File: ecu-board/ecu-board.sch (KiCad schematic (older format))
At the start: 12 parts, among them J1 MicroSquirt_connector, J3 MS_breakout_conn, U1 MAP Sensor

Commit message: Reassign footprints to 0805.
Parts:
- D4, D5: footprint LEDs:LED_D3.0mm -> LEDs:LED_0805_HandSoldering
- R1, R2, R3, R4: footprint Resistors_THT:R_Axial_DIN0309_L9.0mm_D3.2mm_P12.70mm_Horizontal -> Resistors_SMD:R_0805_HandSoldering
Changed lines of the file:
@@
 F 0 "R3" H 8070 1746 50  0000 L CNN
 F 1 "30k" H 8070 1655 50  0000 L CNN
-F 2 "Resistors_THT:R_Axial_DIN0309_L9.0mm_D3.2mm_P12.70mm_Horizontal" V 7930 1700 50  0001 C CNN
+F 2 "Resistors_SMD:R_0805_HandSoldering" V 7930 1700 50  0001 C CNN
 F 3 "~" H 8000 1700 50  0001 C CNN
 	1    8000 1700
@@
 F 0 "R4" H 8070 2146 50  0000 L CNN
 F 1 "30k" H 8070 2055 50  0000 L CNN
-F 2 "Resistors_THT:R_Axial_DIN0309_L9.0mm_D3.2mm_P12.70mm_Horizontal" V 7930 2100 50  0001 C CNN
+F 2 "Resistors_SMD:R_0805_HandSoldering" V 7930 2100 50  0001 C CNN
 F 3 "~" H 8000 2100 50  0001 C CNN
 	1    8000 2100
@@
 F 0 "D4" H 3250 2550 50  0000 C CNN
 F 1 "LED" H 3250 2450 50  0000 C CNN
-F 2 "LEDs:LED_D3.0mm" H 3250 2650 50  0001 C CNN
+F 2 "LEDs:LED_0805_HandSoldering" H 3250 2650 50  0001 C CNN
 F 3 "~" H 3250 2650 50  0001 C CNN
 F 4 "3mm T-1" H 3250 2650 50  0001 C CNN "Part no."
@@
 F 0 "R1" V 3015 2650 50  0000 C CNN
 F 1 "1k" V 3106 2650 50  0000 C CNN
-F 2 "Resistors_THT:R_Axial_DIN0309_L9.0mm_D3.2mm_P12.70mm_Horizontal" V 2830 2650 50  0001 C CNN
+F 2 "Resistors_SMD:R_0805_HandSoldering" V 2830 2650 50  0001 C CNN
 F 3 "~" H 2900 2650 50  0001 C CNN
 	1    2900 2650
@@
 F 0 "D5" H 5350 2500 50  0000 C CNN
 F 1 "LED" H 5350 2400 50  0000 C CNN
-F 2 "LEDs:LED_D3.0mm" H 5350 2600 50  0001 C CNN
+F 2 "LEDs:LED_0805_HandSoldering" H 5350 2600 50  0001 C CNN
 F 3 "~" H 5350 2600 50  0001 C CNN
 F 4 "3mm T-1" H 5350 2600 50  0001 C CNN "Part no."
@@
 F 0 "R2" V 5115 2600 50  0000 C CNN
 F 1 "1k" V 5206 2600 50  0000 C CNN
-F 2 "Resistors_THT:R_Axial_DIN0309_L9.0mm_D3.2mm_P12.70mm_Horizontal" V 4930 2600 50  0001 C CNN
+F 2 "Resistors_SMD:R_0805_HandSoldering" V 4930 2600 50  0001 C CNN
 F 3 "~" H 5000 2600 50  0001 C CNN
 	1    5000 2600

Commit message: Change fuse part no.
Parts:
- F1, F2: Part no. 01530008Z -> 178.4265.0002
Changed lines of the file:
@@
 F 3 "~" H 3200 2500 50  0001 C CNN
 F 4 "Littelfuse" H 3200 2500 50  0001 C CNN "Manufacturer"
-F 5 "01530008Z" H 3200 2500 50  0001 C CNN "Part no."
+F 5 "178.4265.0002" H 3200 2500 50  0001 C CNN "Part no."
 	1    3200 2500
 	1    0    0    -1
@@
 F 3 "~" H 5300 2450 50  0001 C CNN
 F 4 "Littelfuse" H 5300 2450 50  0001 C CNN "Manufacturer"
-F 5 "01530008Z" H 5300 2450 50  0001 C CNN "Part no."
+F 5 "178.4265.0002" H 5300 2450 50  0001 C CNN "Part no."
 	1    5300 2450
 	1    0    0    -1

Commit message: Add fuse holder footprint.
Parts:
- F1, F2: footprint (none) -> ecu-board-footprints:Fuseholder_ATO_Blade_Littelfuse_Pudenz_4_Pin
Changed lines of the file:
@@
 F 0 "F1" H 3200 2685 50  0000 C CNN
 F 1 "3A Fuse" H 3200 2594 50  0000 C CNN
-F 2 "" H 3200 2500 50  0001 C CNN
+F 2 "ecu-board-footprints:Fuseholder_ATO_Blade_Littelfuse_Pudenz_4_Pin" H 3200 2500 50  0001 C CNN
 F 3 "~" H 3200 2500 50  0001 C CNN
 F 4 "Littelfuse" H 3200 2500 50  0001 C CNN "Manufacturer"
@@
 F 0 "F2" H 5300 2635 50  0000 C CNN
 F 1 "5A Fuse" H 5300 2544 50  0000 C CNN
-F 2 "" H 5300 2450 50  0001 C CNN
+F 2 "ecu-board-footprints:Fuseholder_ATO_Blade_Littelfuse_Pudenz_4_Pin" H 5300 2450 50  0001 C CNN
 F 3 "~" H 5300 2450 50  0001 C CNN
 F 4 "Littelfuse" H 5300 2450 50  0001 C CNN "Manufacturer"

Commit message: Add breakout connector.
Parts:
- J3: footprint (none) -> ecu-board-footprints:MicroSquirt_35Pin
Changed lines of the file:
@@
 F 0 "J3" H 4050 6100 50  0000 C CNN
 F 1 "MS_breakout_conn" H 3900 6000 50  0000 C CNN
-F 2 "" H 4150 4150 50  0001 C CNN
+F 2 "ecu-board-footprints:MicroSquirt_35Pin" H 4150 4150 50  0001 C CNN
 F 3 "https://www.phoenixcontact.com/gb/products/1791826" H 4150 4150 50  0001 C CNN
 	1    4150 4150

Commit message: Rename board signals.
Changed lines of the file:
@@
 Comment4 ""
 $EndDescr
-$Sheet
-S 7700 3000 2000 1700
-U 5C5705F6
-F0 "Connectors" 79
-F1 "connectors.sch" 79
-F2 "crankshaft_signal" O R 9700 3150 50
-F3 "camshaft_signal" O R 9700 3350 50
-F4 "ego_signal" O R 9700 3750 50
-F5 "serial_rx" B L 7700 3950 50
-F6 "serial_tx" B L 7700 4150 50
-F7 "injector_input" I L 7700 3150 50
-F8 "clt_signal" O R 9700 3950 50
-F9 "iat_signal" O R 9700 4150 50
-F10 "start_motor_signal" O R 9700 4350 50
-F11 "main_power_signal" O R 9700 4550 50
-F12 "start_motor_power" I L 7700 4550 50
-F13 "ignition1_input" I L 7700 3350 50
-F14 "ignition2_input" I L 7700 3550 50
-F15 "tachometer_input" I L 7700 3750 50
-$EndSheet
 $Comp
 L ecu-board:MicroSquirt_Connector J1
@@
 F1 "relays.sch" 79
 F2 "main_relay_input" I L 7700 5550 50
-F3 "start_motor_relay_input" I L 7700 5800 50
-F4 "start_motor_relay_output" O R 9750 5700 50
+F3 "start_motor_relay_output" O R 9750 5700 50
+F4 "~start_motor_relay_input~" I L 7700 5800 50
 $EndSheet
 Text Label 9950 5700 0    50   ~ 0
@@
 Wire Wire Line
 	4750 3850 4350 3850
+$Sheet
+S 7700 3000 2000 1700
+U 5C5705F6
+F0 "Connectors" 79
+F1 "connectors.sch" 79
+F2 "crankshaft_signal" O R 9700 3150 50
+F3 "camshaft_signal" O R 9700 3350 50
+F4 "ego_signal" O R 9700 3750 50
+F5 "serial_rx" B L 7700 3950 50
+F6 "serial_tx" B L 7700 4150 50
+F7 "injector_input" I L 7700 3150 50
+F8 "clt_signal" O R 9700 3950 50
+F9 "iat_signal" O R 9700 4150 50
+F10 "main_power_signal" O R 9700 4550 50
+F11 "start_motor_power" I L 7700 4550 50
+F12 "ignition1_input" I L 7700 3350 50
+F13 "ignition2_input" I L 7700 3550 50
+F14 "tachometer" O L 7700 3750 50
+F15 "~start_motor_signal~" O R 9700 4350 50
+$EndSheet
 $EndSCHEMATC

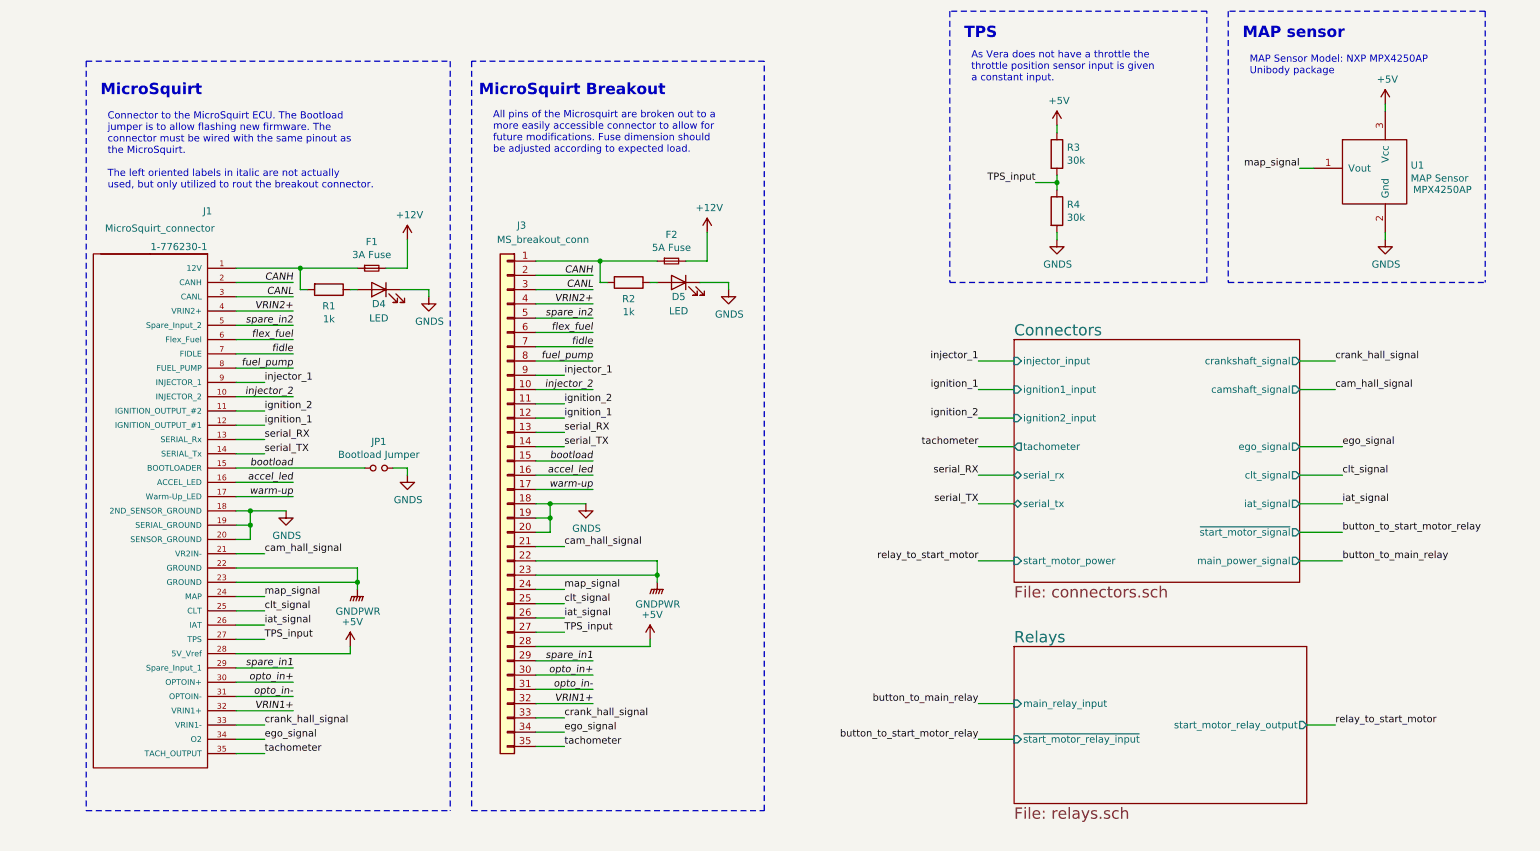
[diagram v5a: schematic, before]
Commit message: Add CAN connector.
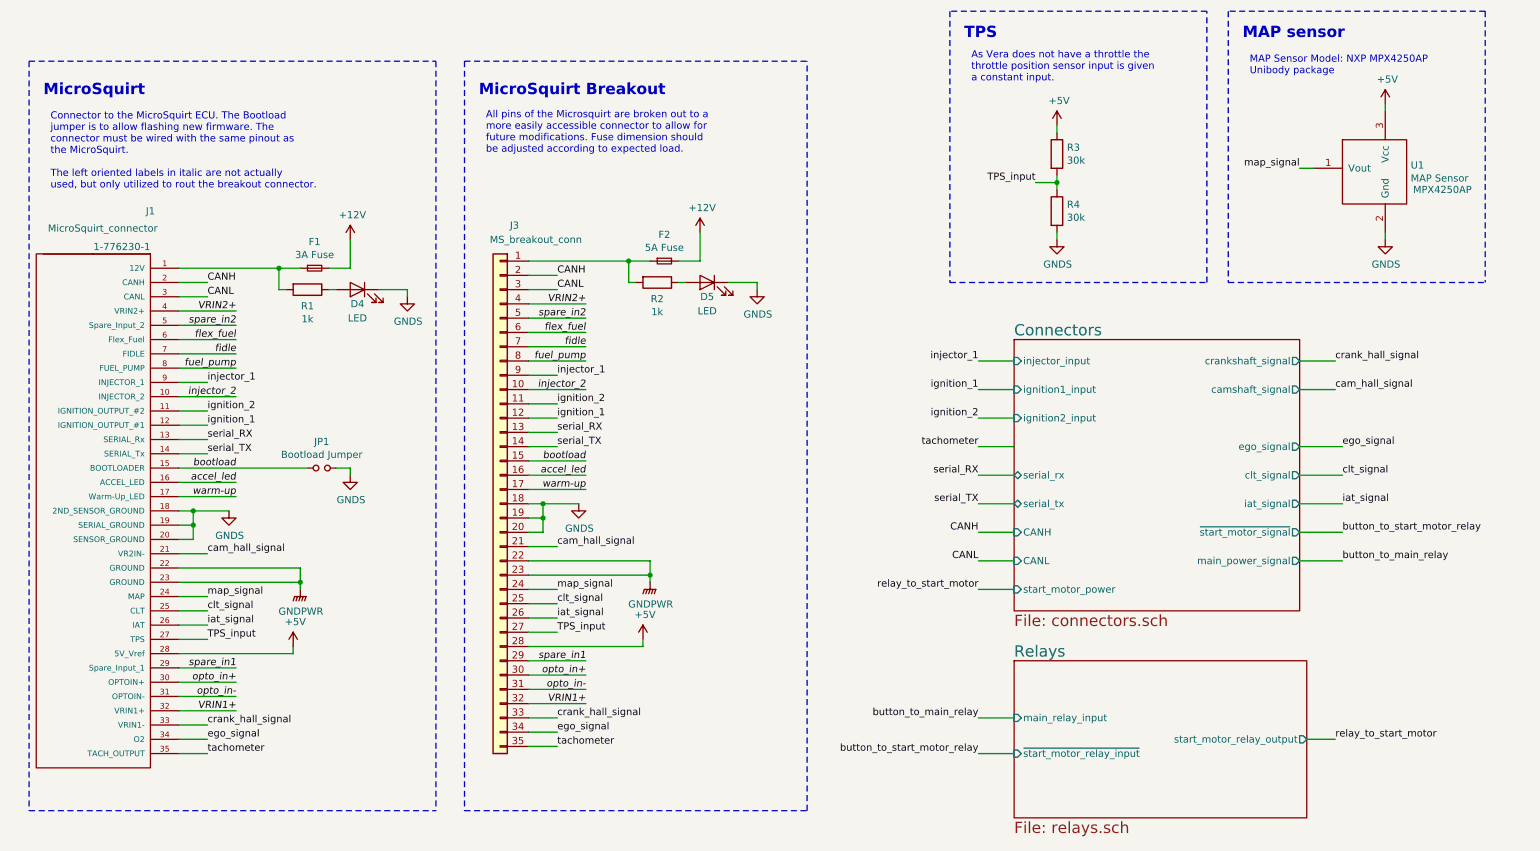
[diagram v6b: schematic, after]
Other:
- moved on the sheet: D4, D5, F1, F2, J1, J3, JP1, R1, R2

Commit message: Add speed sensor connector.
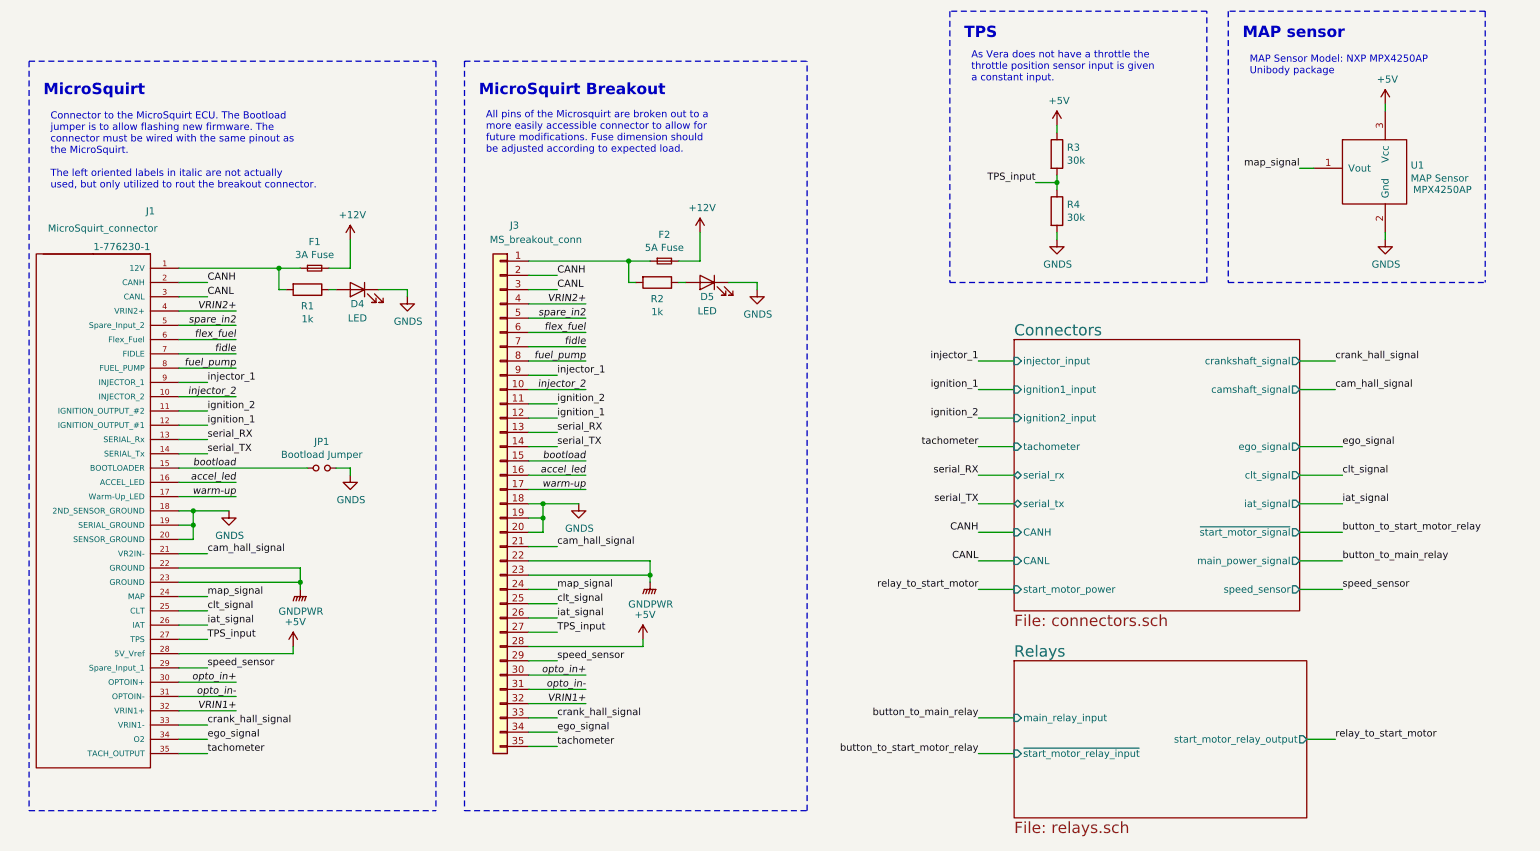
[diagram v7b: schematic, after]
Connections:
- net spare_in1 renamed speed_sensor
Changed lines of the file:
@@
 Wire Wire Line
 	2250 4100 1850 4100
-Text Label 2250 5300 2    50   Italic 0
-spare_in1
-Wire Wire Line
-	2250 5300 1850 5300
 Text Label 2250 5400 2    50   Italic 0
 opto_in+
@@
 Wire Wire Line
 	4700 4050 4300 4050
-Text Label 4700 5250 2    50   Italic 0
-spare_in1
-Wire Wire Line
-	4700 5250 4300 5250
 Text Label 4700 5350 2    50   Italic 0
 opto_in+
@@
 F15 "CANH" I L 7700 4350 50
 F16 "CANL" I L 7700 4550 50
+F17 "tachometer" I L 7700 3750 50
+F18 "speed_sensor" O R 9700 4750 50
 $EndSheet
 Wire Wire Line
@@
 Wire Notes Line
 	3850 1050 6250 1050
+Text Label 10000 4750 0    50   ~ 0
+speed_sensor
+Wire Wire Line
+	10000 4750 9700 4750
+Text Label 2050 5300 0    50   ~ 0
+speed_sensor
+Wire Wire Line
+	2050 5300 1850 5300
+Text Label 4500 5250 0    50   ~ 0
+speed_sensor
+Wire Wire Line
+	4500 5250 4300 5250
 $EndSCHEMATC
